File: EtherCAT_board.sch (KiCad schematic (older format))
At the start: 26 parts, among them J1 CONN_01X12, J2 USB_OTG, J3 RJ45-PULSETRANS, J4 RJ45-PULSETRANS, SW1 SKRPACE010, U1 LAN9252, U2 LM1117-3.3

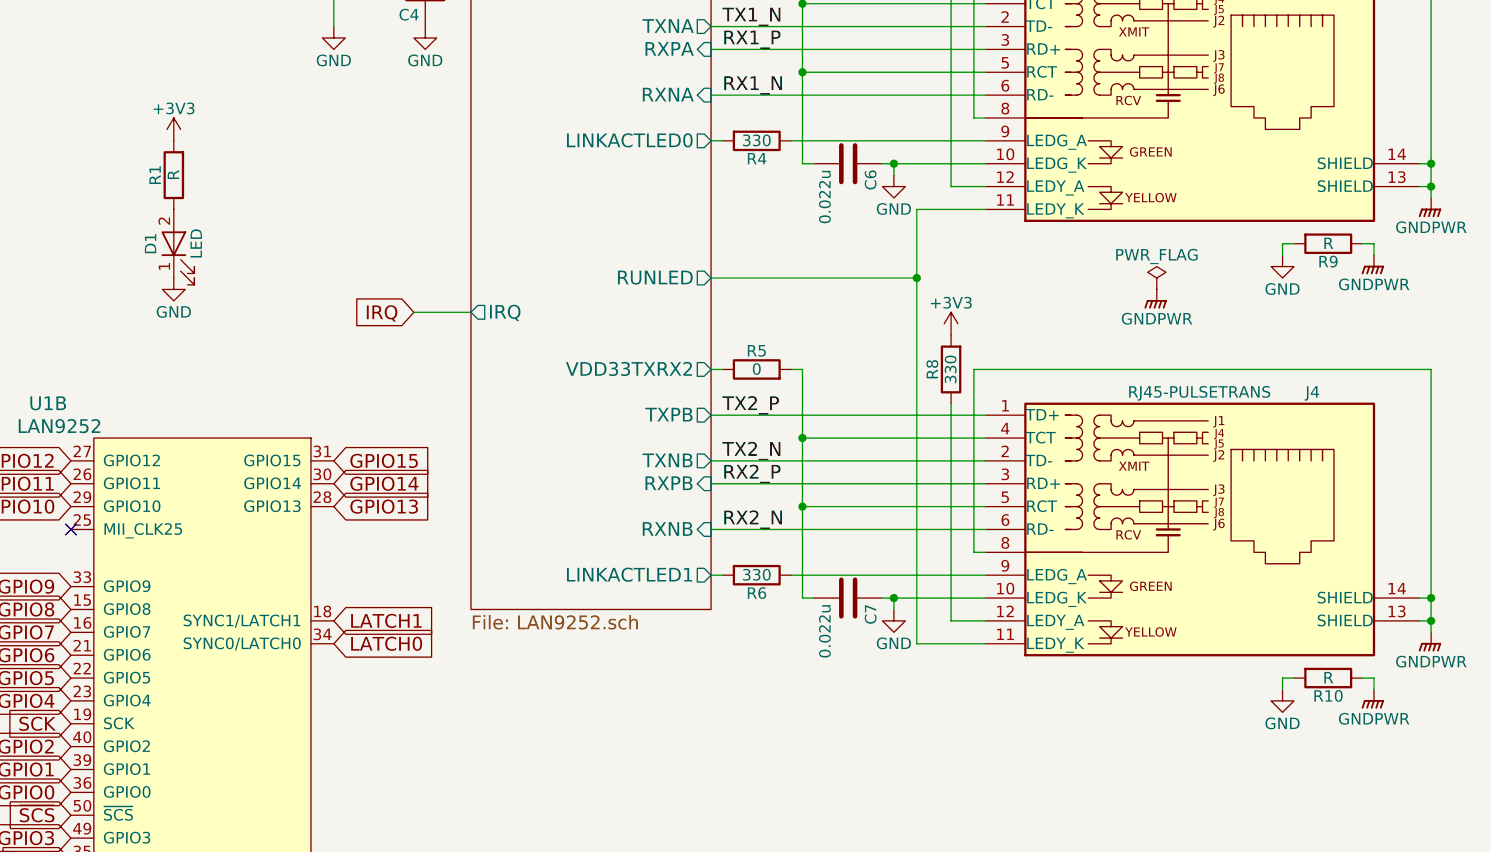
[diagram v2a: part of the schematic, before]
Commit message: フットプリント割当 基板作成開始
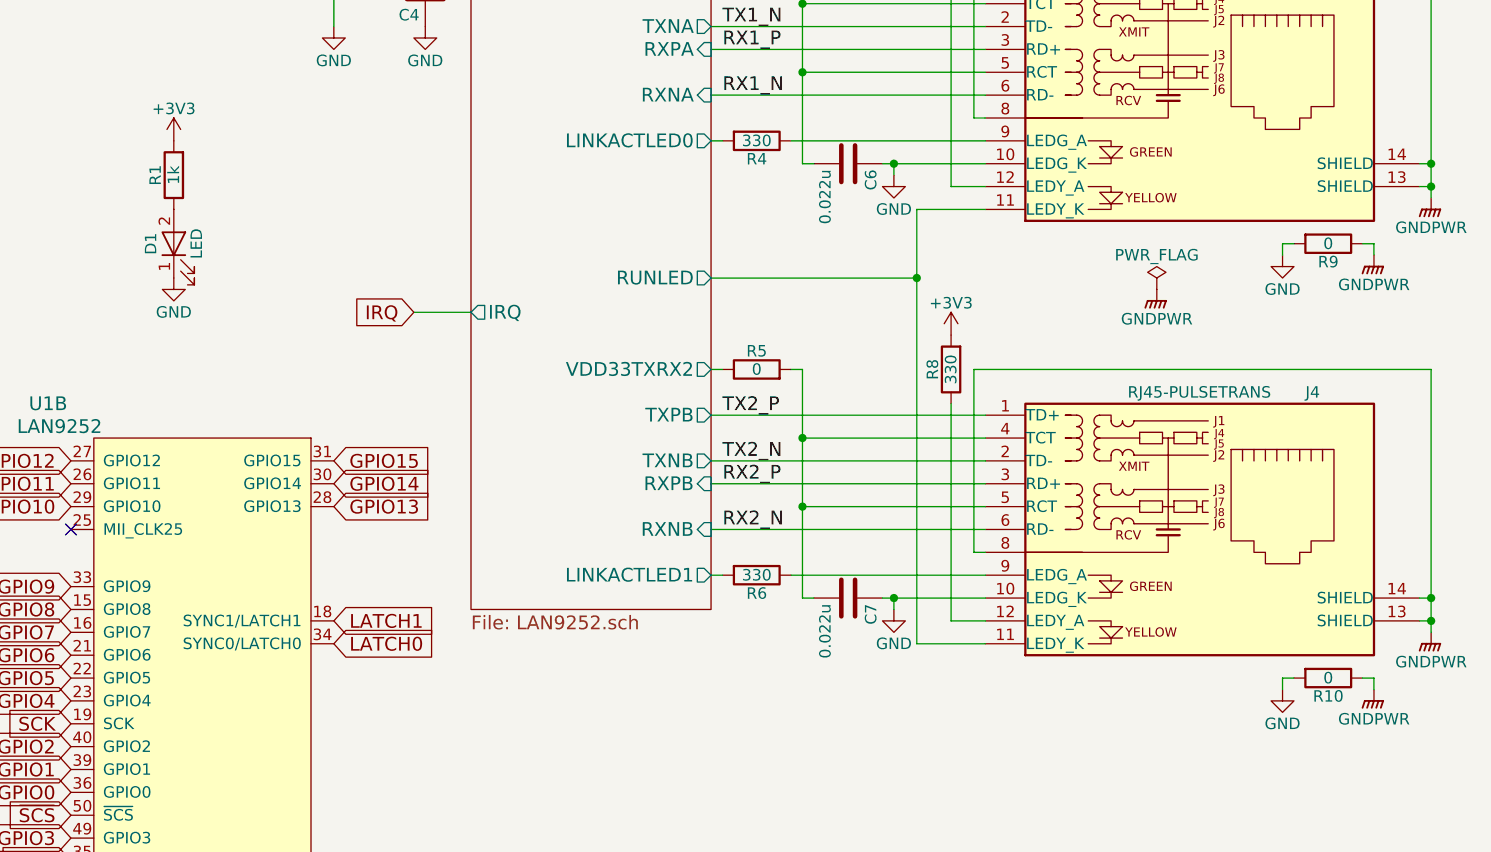
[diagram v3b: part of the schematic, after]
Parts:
- C1, C2, C3, C4, C5, C6, C7: footprint (none) -> Capacitors_SMD:C_0603
- D1: footprint (none) -> LEDs:LED_0603
- F1: footprint (none) -> Resistors_SMD:R_2816
- J1: footprint (none) -> Pin_Headers:Pin_Header_Straight_1x12_Pitch2.54mm
- J2: footprint (none) -> Connect:USB_Micro-B
- J3, J4: footprint (none) -> Connect:RJ45_J0011D21BNL
- R1: value R -> 1k; footprint (none) -> Resistors_SMD:R_0603
- R10, R9: value R -> 0; footprint (none) -> Resistors_SMD:R_1210
- R2, R3, R4, R5, R6, R7, R8: footprint (none) -> Resistors_SMD:R_0603
- SW1: footprint (none) -> SMD_Packages:ALPS_SKRPAxE010
- U1: footprint (none) -> Housings_DFN_QFN:QFN-64-1EP_9x9mm_Pitch0.5mm_LAN9252
- U2: footprint (none) -> TO_SOT_Packages_SMD:SOT-223-3Lead_TabPin2
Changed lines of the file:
@@
 F 0 "R8" V 8930 4850 50  0000 C CNN
 F 1 "330" V 8850 4850 50  0000 C CNN
-F 2 "" V 8780 4850 50  0001 C CNN
+F 2 "Resistors_SMD:R_0603" V 8780 4850 50  0001 C CNN
 F 3 "" H 8850 4850 50  0001 C CNN
 	1    8850 4850
@@
 F 0 "R7" V 8930 2950 50  0000 C CNN
 F 1 "330" V 8850 2950 50  0000 C CNN
-F 2 "" V 8780 2950 50  0001 C CNN
+F 2 "Resistors_SMD:R_0603" V 8780 2950 50  0001 C CNN
 F 3 "" H 8850 2950 50  0001 C CNN
 	1    8850 2950
@@
 F 0 "J3" H 10400 4250 50  0000 L CNN
 F 1 "RJ45-PULSETRANS" H 10250 4250 50  0000 R CNN
-F 2 "" H 10300 3650 50  0001 C CNN
+F 2 "Connect:RJ45_J0011D21BNL" H 10300 3650 50  0001 C CNN
 F 3 "" H 10300 3650 50  0001 C CNN
 	1    10300 3650
@@
 F 0 "J4" H 10400 6150 50  0000 L CNN
 F 1 "RJ45-PULSETRANS" H 10250 6150 50  0000 R CNN
-F 2 "" H 10300 5550 50  0001 C CNN
+F 2 "Connect:RJ45_J0011D21BNL" H 10300 5550 50  0001 C CNN
 F 3 "" H 10300 5550 50  0001 C CNN
 	1    10300 5550
@@
 P 10500 4300
 F 0 "R9" V 10580 4300 50  0000 C CNN
-F 1 "R" V 10500 4300 50  0000 C CNN
-F 2 "" V 10430 4300 50  0001 C CNN
+F 1 "0" V 10500 4300 50  0000 C CNN
+F 2 "Resistors_SMD:R_1210" V 10430 4300 50  0001 C CNN
 F 3 "" H 10500 4300 50  0001 C CNN
 	1    10500 4300
@@
 P 10500 6200
 F 0 "R10" V 10580 6200 50  0000 C CNN
-F 1 "R" V 10500 6200 50  0000 C CNN
-F 2 "" V 10430 6200 50  0001 C CNN
+F 1 "0" V 10500 6200 50  0000 C CNN
+F 2 "Resistors_SMD:R_1210" V 10430 6200 50  0001 C CNN
 F 3 "" H 10500 6200 50  0001 C CNN
 	1    10500 6200
@@
 F 0 "R3" V 8080 2950 50  0000 C CNN
 F 1 "0" V 8000 2950 50  0000 C CNN
-F 2 "" V 7930 2950 50  0001 C CNN
+F 2 "Resistors_SMD:R_0603" V 7930 2950 50  0001 C CNN
 F 3 "" H 8000 2950 50  0001 C CNN
 	1    8000 2950
@@
 F 0 "R4" V 8080 3850 50  0000 C CNN
 F 1 "330" V 8000 3850 50  0000 C CNN
-F 2 "" V 7930 3850 50  0001 C CNN
+F 2 "Resistors_SMD:R_0603" V 7930 3850 50  0001 C CNN
 F 3 "" H 8000 3850 50  0001 C CNN
 	1    8000 3850
@@
 F 0 "C6" H 8425 4050 50  0000 L CNN
 F 1 "0.022u" H 8425 3850 50  0000 L CNN
-F 2 "" H 8438 3800 50  0001 C CNN
+F 2 "Capacitors_SMD:C_0603" H 8438 3800 50  0001 C CNN
 F 3 "" H 8400 3950 50  0001 C CNN
 	1    8400 3950
@@
 F 0 "R6" V 8080 5750 50  0000 C CNN
 F 1 "330" V 8000 5750 50  0000 C CNN
-F 2 "" V 7930 5750 50  0001 C CNN
+F 2 "Resistors_SMD:R_0603" V 7930 5750 50  0001 C CNN
 F 3 "" H 8000 5750 50  0001 C CNN
 	1    8000 5750
@@
 F 0 "R5" V 8080 4850 50  0000 C CNN
 F 1 "0" V 8000 4850 50  0000 C CNN
-F 2 "" V 7930 4850 50  0001 C CNN
+F 2 "Resistors_SMD:R_0603" V 7930 4850 50  0001 C CNN
 F 3 "" H 8000 4850 50  0001 C CNN
 	1    8000 4850
@@
 F 0 "C7" H 8425 5950 50  0000 L CNN
 F 1 "0.022u" H 8425 5750 50  0000 L CNN
-F 2 "" H 8438 5700 50  0001 C CNN
+F 2 "Capacitors_SMD:C_0603" H 8438 5700 50  0001 C CNN
 F 3 "" H 8400 5850 50  0001 C CNN
 	1    8400 5850
@@
 F 0 "R2" V 6630 2700 50  0000 C CNN
 F 1 "10k" V 6550 2700 50  0000 C CNN
-F 2 "" V 6480 2700 50  0001 C CNN
+F 2 "Resistors_SMD:R_0603" V 6480 2700 50  0001 C CNN
 F 3 "" H 6550 2700 50  0001 C CNN
 	1    6550 2700
@@
 F 0 "C4" H 6575 3300 50  0000 L CNN
 F 1 "0.1u" H 6575 3100 50  0000 L CNN
-F 2 "" H 6588 3050 50  0001 C CNN
+F 2 "Capacitors_SMD:C_0603" H 6588 3050 50  0001 C CNN
 F 3 "" H 6550 3200 50  0001 C CNN
 	1    6550 3200
@@
 F 0 "J2" H 4950 1800 50  0000 L CNN
 F 1 "USB_OTG" H 4950 1700 50  0000 L CNN
-F 2 "" H 5300 1300 50  0001 C CNN
+F 2 "Connect:USB_Micro-B" H 5300 1300 50  0001 C CNN
 F 3 "" H 5300 1300 50  0001 C CNN
 	1    5150 1350
@@
 F 0 "F1" V 5780 1150 50  0000 C CNN
 F 1 "Fuse" V 5625 1150 50  0000 C CNN
-F 2 "" V 5630 1150 50  0001 C CNN
+F 2 "Resistors_SMD:R_2816" V 5630 1150 50  0001 C CNN
 F 3 "" H 5700 1150 50  0001 C CNN
 	1    5700 1150
@@
 F 0 "SW1" H 5850 3200 50  0000 C CNN
 F 1 "SKRPACE010" H 5850 2900 50  0000 C CNN
-F 2 "" V 5800 3050 60  0000 C CNN
+F 2 "SMD_Packages:ALPS_SKRPAxE010" V 5800 3050 60  0001 C CNN
 F 3 "" V 5800 3050 60  0000 C CNN
 	1    5850 3050
@@
 F 0 "U1" H 5300 5300 60  0000 C CNN
 F 1 "LAN9252" H 5250 5200 60  0000 C CNN
-F 2 "" H 3850 4100 60  0001 C CNN
+F 2 "Housings_DFN_QFN:QFN-64-1EP_9x9mm_Pitch0.5mm_LAN9252" H 3850 4100 60  0001 C CNN
 F 3 "" H 3850 4100 60  0001 C CNN
 	2    5100 5150
@@
 F 0 "D1" H 5450 4400 50  0000 C CNN
 F 1 "LED" H 5450 4200 50  0000 C CNN
-F 2 "" H 5450 4300 50  0001 C CNN
+F 2 "LEDs:LED_0603" H 5450 4300 50  0001 C CNN
 F 3 "" H 5450 4300 50  0001 C CNN
 	1    5450 4300
@@
 P 5450 4000
 F 0 "R1" V 5530 4000 50  0000 C CNN
-F 1 "R" V 5450 4000 50  0000 C CNN
-F 2 "" V 5380 4000 50  0001 C CNN
+F 1 "1k" V 5450 4000 50  0000 C CNN
+F 2 "Resistors_SMD:R_0603" V 5380 4000 50  0001 C CNN
 F 3 "" H 5450 4000 50  0001 C CNN
 	1    5450 4000
@@
 F 0 "J1" H 2050 7000 50  0000 C CNN
 F 1 "CONN_01X12" V 2150 6350 50  0000 C CNN
-F 2 "" H 2050 6350 50  0001 C CNN
+F 2 "Pin_Headers:Pin_Header_Straight_1x12_Pitch2.54mm" H 2050 6350 50  0001 C CNN
 F 3 "" H 2050 6350 50  0001 C CNN
 	1    2050 6350
@@
 F 0 "C1" H 3175 6950 50  0000 L CNN
 F 1 "22u" H 3175 6750 50  0000 L CNN
-F 2 "" H 3188 6700 50  0001 C CNN
+F 2 "Capacitors_SMD:C_0603" H 3188 6700 50  0001 C CNN
 F 3 "" H 3150 6850 50  0001 C CNN
 	1    3150 6850
@@
 F 0 "C2" H 3375 6950 50  0000 L CNN
 F 1 "22u" H 3375 6750 50  0000 L CNN
-F 2 "" H 3388 6700 50  0001 C CNN
+F 2 "Capacitors_SMD:C_0603" H 3388 6700 50  0001 C CNN
 F 3 "" H 3350 6850 50  0001 C CNN
 	1    3350 6850
@@
 F 0 "U2" H 6800 900 50  0000 C CNN
 F 1 "LM1117-3.3" H 6700 1400 50  0000 C CNN
-F 2 "" H 6700 1150 50  0001 C CNN
+F 2 "TO_SOT_Packages_SMD:SOT-223-3Lead_TabPin2" H 6700 1150 50  0001 C CNN
 F 3 "" H 6700 1150 50  0001 C CNN
 	1    6700 1150
@@
 F 0 "C5" H 7125 1500 50  0000 L CNN
 F 1 "22u" H 7125 1300 50  0000 L CNN
-F 2 "" H 7138 1250 50  0001 C CNN
+F 2 "Capacitors_SMD:C_0603" H 7138 1250 50  0001 C CNN
 F 3 "" H 7100 1400 50  0001 C CNN
 	1    7100 1400
@@
 F 0 "C3" H 6275 1500 50  0000 L CNN
 F 1 "10u" H 6275 1300 50  0000 L CNN
-F 2 "" H 6288 1250 50  0001 C CNN
+F 2 "Capacitors_SMD:C_0603" H 6288 1250 50  0001 C CNN
 F 3 "" H 6250 1400 50  0001 C CNN
 	1    6250 1400

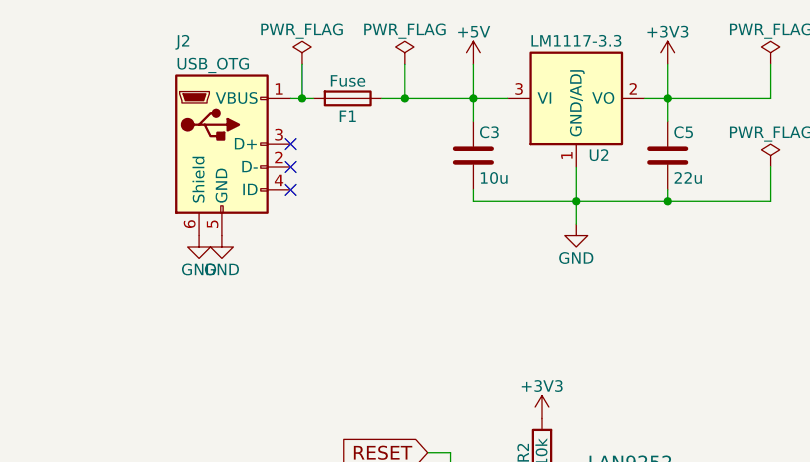
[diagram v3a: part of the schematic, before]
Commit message: 5Vの電源LEDを追加 ポリスイッチのサイズを3225に変更
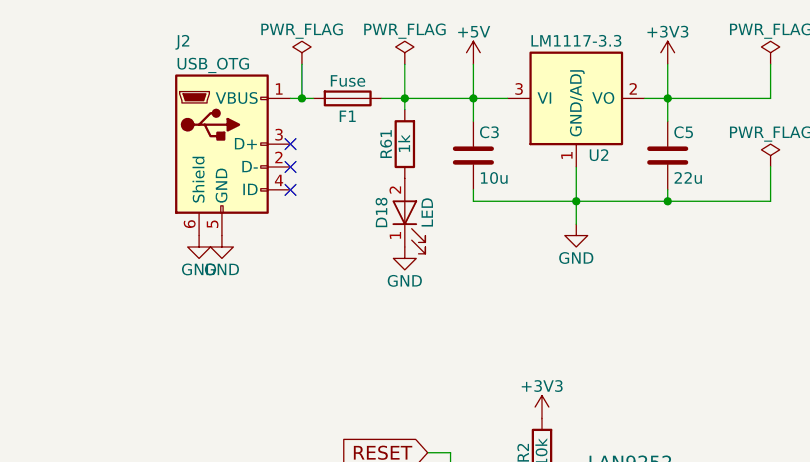
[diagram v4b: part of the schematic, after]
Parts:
- added D18: LED, LEDs:LED_0603, symbol LED
- added R61: 1k, Resistors_SMD:R_0603, symbol R
- F1: footprint Resistors_SMD:R_2816 -> Resistors_SMD:R_1210
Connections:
- net +5V: now also R61.2
- net GND: now also D18.1 (K)
- new net: D18.2 (A), R61.1
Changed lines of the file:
@@
 EESchema Schematic File Version 2
+LIBS:EtherCAT_board-rescue
 LIBS:power
 LIBS:device
@@
 $EndComp
 $Comp
-L +3V3 #PWR01
+L +3V3 #PWR17
 U 1 1 5922F51B
 P 8850 4700
-F 0 "#PWR01" H 8850 4550 50  0001 C CNN
+F 0 "#PWR17" H 8850 4550 50  0001 C CNN
 F 1 "+3V3" H 8850 4840 50  0000 C CNN
 F 2 "" H 8850 4700 50  0001 C CNN
@@
 $EndComp
 $Comp
-L +3V3 #PWR02
+L +3V3 #PWR16
 U 1 1 5922FF45
 P 8850 2800
-F 0 "#PWR02" H 8850 2650 50  0001 C CNN
+F 0 "#PWR16" H 8850 2650 50  0001 C CNN
 F 1 "+3V3" H 8850 2940 50  0000 C CNN
 F 2 "" H 8850 2800 50  0001 C CNN
@@
 $EndComp
 $Comp
-L GND #PWR03
+L GND #PWR19
 U 1 1 5922FEB9
 P 10300 4350
-F 0 "#PWR03" H 10300 4100 50  0001 C CNN
+F 0 "#PWR19" H 10300 4100 50  0001 C CNN
 F 1 "GND" H 10300 4200 50  0000 C CNN
 F 2 "" H 10300 4350 50  0001 C CNN
@@
 $EndComp
 $Comp
-L GNDPWR #PWR04
+L GNDPWR #PWR21
 U 1 1 5922FF05
 P 10700 4350
-F 0 "#PWR04" H 10700 4150 50  0001 C CNN
+F 0 "#PWR21" H 10700 4150 50  0001 C CNN
 F 1 "GNDPWR" H 10700 4220 50  0000 C CNN
 F 2 "" H 10700 4300 50  0001 C CNN
@@
 $EndComp
 $Comp
-L GNDPWR #PWR05
+L GNDPWR #PWR22
 U 1 1 5923028E
 P 10700 6250
-F 0 "#PWR05" H 10700 6050 50  0001 C CNN
+F 0 "#PWR22" H 10700 6050 50  0001 C CNN
 F 1 "GNDPWR" H 10700 6120 50  0000 C CNN
 F 2 "" H 10700 6200 50  0001 C CNN
@@
 $EndComp
 $Comp
-L GND #PWR06
+L GND #PWR20
 U 1 1 5923041F
 P 10300 6250
-F 0 "#PWR06" H 10300 6000 50  0001 C CNN
+F 0 "#PWR20" H 10300 6000 50  0001 C CNN
 F 1 "GND" H 10300 6100 50  0000 C CNN
 F 2 "" H 10300 6250 50  0001 C CNN
@@
 $EndComp
 $Comp
-L GNDPWR #PWR07
+L GNDPWR #PWR23
 U 1 1 592307DA
 P 10950 4100
-F 0 "#PWR07" H 10950 3900 50  0001 C CNN
+F 0 "#PWR23" H 10950 3900 50  0001 C CNN
 F 1 "GNDPWR" H 10950 3970 50  0000 C CNN
 F 2 "" H 10950 4050 50  0001 C CNN
@@
 $EndComp
 $Comp
-L GNDPWR #PWR08
+L GNDPWR #PWR24
 U 1 1 5923094F
 P 10950 6000
-F 0 "#PWR08" H 10950 5800 50  0001 C CNN
+F 0 "#PWR24" H 10950 5800 50  0001 C CNN
 F 1 "GNDPWR" H 10950 5870 50  0000 C CNN
 F 2 "" H 10950 5950 50  0001 C CNN
@@
 $EndComp
 $Comp
-L GND #PWR09
+L GND #PWR14
 U 1 1 592A4371
 P 8600 4000
-F 0 "#PWR09" H 8600 3750 50  0001 C CNN
+F 0 "#PWR14" H 8600 3750 50  0001 C CNN
 F 1 "GND" H 8600 3850 50  0000 C CNN
 F 2 "" H 8600 4000 50  0001 C CNN
@@
 $EndComp
 $Comp
-L GND #PWR010
+L GND #PWR15
 U 1 1 592A4F5E
 P 8600 5900
-F 0 "#PWR010" H 8600 5650 50  0001 C CNN
+F 0 "#PWR15" H 8600 5650 50  0001 C CNN
 F 1 "GND" H 8600 5750 50  0000 C CNN
 F 2 "" H 8600 5900 50  0001 C CNN
@@
 $EndComp
 $Comp
-L +3V3 #PWR011
+L +3V3 #PWR10
 U 1 1 592B3DAC
 P 6550 2550
-F 0 "#PWR011" H 6550 2400 50  0001 C CNN
+F 0 "#PWR10" H 6550 2400 50  0001 C CNN
 F 1 "+3V3" H 6550 2690 50  0000 C CNN
 F 2 "" H 6550 2550 50  0001 C CNN
@@
 $EndComp
 $Comp
-L GND #PWR012
+L GND #PWR11
 U 1 1 592B401A
 P 6550 3350
-F 0 "#PWR012" H 6550 3100 50  0001 C CNN
+F 0 "#PWR11" H 6550 3100 50  0001 C CNN
 F 1 "GND" H 6550 3200 50  0000 C CNN
 F 2 "" H 6550 3350 50  0001 C CNN
@@
 $EndComp
 $Comp
-L GND #PWR013
+L GND #PWR3
 U 1 1 59240EF6
 P 5050 1750
-F 0 "#PWR013" H 5050 1500 50  0001 C CNN
+F 0 "#PWR3" H 5050 1500 50  0001 C CNN
 F 1 "GND" H 5050 1600 50  0000 C CNN
 F 2 "" H 5050 1750 50  0001 C CNN
@@
 $EndComp
 $Comp
-L GND #PWR014
+L GND #PWR4
 U 1 1 59242075
 P 5150 1750
-F 0 "#PWR014" H 5150 1500 50  0001 C CNN
+F 0 "#PWR4" H 5150 1500 50  0001 C CNN
 F 1 "GND" H 5150 1600 50  0000 C CNN
 F 2 "" H 5150 1750 50  0001 C CNN
@@
 F 0 "F1" V 5780 1150 50  0000 C CNN
 F 1 "Fuse" V 5625 1150 50  0000 C CNN
-F 2 "Resistors_SMD:R_2816" V 5630 1150 50  0001 C CNN
+F 2 "Resistors_SMD:R_1210" V 5630 1150 50  0001 C CNN
 F 3 "" H 5700 1150 50  0001 C CNN
 	1    5700 1150
@@
 NoConn ~ 5650 3150
 $Comp
-L GND #PWR015
+L GND #PWR8
 U 1 1 592521B8
 P 6150 3350
-F 0 "#PWR015" H 6150 3100 50  0001 C CNN
+F 0 "#PWR8" H 6150 3100 50  0001 C CNN
 F 1 "GND" H 6150 3200 50  0000 C CNN
 F 2 "" H 6150 3350 50  0001 C CNN
@@
 IRQ
 $Comp
-L +3V3 #PWR016
+L +3V3 #PWR5
 U 1 1 5927681F
 P 5450 3850
-F 0 "#PWR016" H 5450 3700 50  0001 C CNN
+F 0 "#PWR5" H 5450 3700 50  0001 C CNN
 F 1 "+3V3" H 5450 3990 50  0000 C CNN
 F 2 "" H 5450 3850 50  0001 C CNN
@@
 $EndComp
 $Comp
-L GND #PWR017
+L GND #PWR6
 U 1 1 59277FBB
 P 5450 4450
-F 0 "#PWR017" H 5450 4200 50  0001 C CNN
+F 0 "#PWR6" H 5450 4200 50  0001 C CNN
 F 1 "GND" H 5450 4300 50  0000 C CNN
 F 2 "" H 5450 4450 50  0001 C CNN
@@
 SIO3
 $Comp
-L +3V3 #PWR018
+L +3V3 #PWR1
 U 1 1 5928CFF9
 P 3000 6600
-F 0 "#PWR018" H 3000 6450 50  0001 C CNN
+F 0 "#PWR1" H 3000 6450 50  0001 C CNN
 F 1 "+3V3" H 3000 6740 50  0000 C CNN
 F 2 "" H 3000 6600 50  0001 C CNN
@@
 $EndComp
 $Comp
-L GND #PWR019
+L GND #PWR2
 U 1 1 5928E4C7
 P 3000 7100
-F 0 "#PWR019" H 3000 6850 50  0001 C CNN
+F 0 "#PWR2" H 3000 6850 50  0001 C CNN
 F 1 "GND" H 3000 6950 50  0000 C CNN
 F 2 "" H 3000 7100 50  0001 C CNN
@@
 $EndComp
 $Comp
-L +5V #PWR020
+L +5V #PWR9
 U 1 1 592C88B8
 P 6250 1000
-F 0 "#PWR020" H 6250 850 50  0001 C CNN
+F 0 "#PWR9" H 6250 850 50  0001 C CNN
 F 1 "+5V" H 6250 1140 50  0000 C CNN
 F 2 "" H 6250 1000 50  0001 C CNN
@@
 $EndComp
 $Comp
-L +3V3 #PWR021
+L +3V3 #PWR13
 U 1 1 592C980E
 P 7100 1000
-F 0 "#PWR021" H 7100 850 50  0001 C CNN
+F 0 "#PWR13" H 7100 850 50  0001 C CNN
 F 1 "+3V3" H 7100 1140 50  0000 C CNN
 F 2 "" H 7100 1000 50  0001 C CNN
@@
 Connection ~ 6700 1600
 $Comp
-L GND #PWR022
+L GND #PWR12
 U 1 1 592CCB1A
 P 6700 1700
-F 0 "#PWR022" H 6700 1450 50  0001 C CNN
+F 0 "#PWR12" H 6700 1450 50  0001 C CNN
 F 1 "GND" H 6700 1550 50  0000 C CNN
 F 2 "" H 6700 1700 50  0001 C CNN
@@
 	5850 1150 6400 1150
 $Comp
-L PWR_FLAG #FLG023
+L PWR_FLAG #FLG3
 U 1 1 592D234F
 P 7550 1000
-F 0 "#FLG023" H 7550 1075 50  0001 C CNN
+F 0 "#FLG3" H 7550 1075 50  0001 C CNN
 F 1 "PWR_FLAG" H 7550 1150 50  0000 C CNN
 F 2 "" H 7550 1000 50  0001 C CNN
@@
 	7550 1150 7550 1000
 $Comp
-L PWR_FLAG #FLG024
+L PWR_FLAG #FLG4
 U 1 1 592D2BA7
 P 7550 1450
-F 0 "#FLG024" H 7550 1525 50  0001 C CNN
+F 0 "#FLG4" H 7550 1525 50  0001 C CNN
 F 1 "PWR_FLAG" H 7550 1600 50  0000 C CNN
 F 2 "" H 7550 1450 50  0001 C CNN
@@
 Connection ~ 7100 1600
 $Comp
-L GNDPWR #PWR025
+L GNDPWR #PWR18
 U 1 1 592D7825
 P 9750 4500
-F 0 "#PWR025" H 9750 4300 50  0001 C CNN
+F 0 "#PWR18" H 9750 4300 50  0001 C CNN
 F 1 "GNDPWR" H 9750 4370 50  0000 C CNN
 F 2 "" H 9750 4450 50  0001 C CNN
@@
 $EndComp
 $Comp
-L PWR_FLAG #FLG026
+L PWR_FLAG #FLG5
 U 1 1 592D7B3F
 P 9750 4500
-F 0 "#FLG026" H 9750 4575 50  0001 C CNN
+F 0 "#FLG5" H 9750 4575 50  0001 C CNN
 F 1 "PWR_FLAG" H 9750 4650 50  0000 C CNN
 F 2 "" H 9750 4500 50  0001 C CNN
@@
 $EndComp
 $Comp
-L PWR_FLAG #FLG027
+L PWR_FLAG #FLG2
 U 1 1 592D7C8B
 P 5950 1000
-F 0 "#FLG027" H 5950 1075 50  0001 C CNN
+F 0 "#FLG2" H 5950 1075 50  0001 C CNN
 F 1 "PWR_FLAG" H 5950 1150 50  0000 C CNN
 F 2 "" H 5950 1000 50  0001 C CNN
@@
 $EndComp
 Wire Wire Line
-	5950 1000 5950 1150
+	5950 1000 5950 1200
 Connection ~ 5950 1150
 $Comp
-L PWR_FLAG #FLG028
+L PWR_FLAG #FLG1
 U 1 1 592D8703
 P 5500 1000
-F 0 "#FLG028" H 5500 1075 50  0001 C CNN
+F 0 "#FLG1" H 5500 1075 50  0001 C CNN
 F 1 "PWR_FLAG" H 5500 1150 50  0000 C CNN
 F 2 "" H 5500 1000 50  0001 C CNN
@@
 	5500 1000 5500 1150
 Connection ~ 5500 1150
+$Comp
+L GND #PWR7
+U 1 1 592B099F
+P 5950 1800
+F 0 "#PWR7" H 5950 1550 50  0001 C CNN
+F 1 "GND" H 5950 1650 50  0000 C CNN
+F 2 "" H 5950 1800 50  0001 C CNN
+F 3 "" H 5950 1800 50  0001 C CNN
+	1    5950 1800
+	1    0    0    -1
+$EndComp
+$Comp
+L LED D18
+U 1 1 592B4592
+P 5950 1650
+F 0 "D18" H 5950 1750 50  0000 C CNN
+F 1 "LED" H 5950 1550 50  0000 C CNN
+F 2 "LEDs:LED_0603" H 5950 1650 50  0001 C CNN
+F 3 "" H 5950 1650 50  0001 C CNN
+	1    5950 1650
+	0    -1   -1   0
+$EndComp
+$Comp
+L R R61
+U 1 1 592B4598
+P 5950 1350
+F 0 "R61" V 6030 1350 50  0000 C CNN
+F 1 "1k" V 5950 1350 50  0000 C CNN
+F 2 "Resistors_SMD:R_0603" V 5880 1350 50  0001 C CNN
+F 3 "" H 5950 1350 50  0001 C CNN
+	1    5950 1350
+	-1   0    0    1
+$EndComp
 $EndSCHEMATC
